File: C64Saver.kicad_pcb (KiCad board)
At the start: 2 copper layers, 33.3 x 43.2 mm, 16 parts, among them J1 Power I/O, Q1 PN2222A, Q2 PN2222A

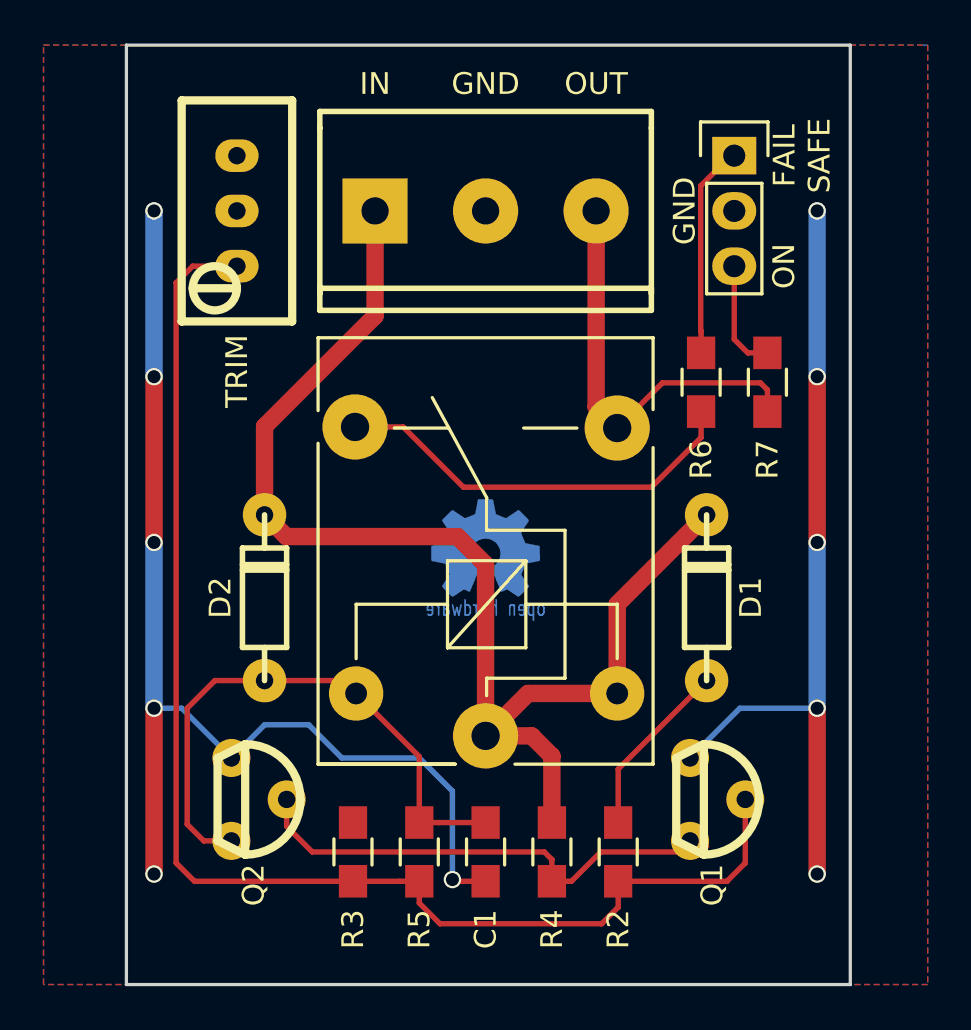
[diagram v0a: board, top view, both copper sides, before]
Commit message: Relabel some components
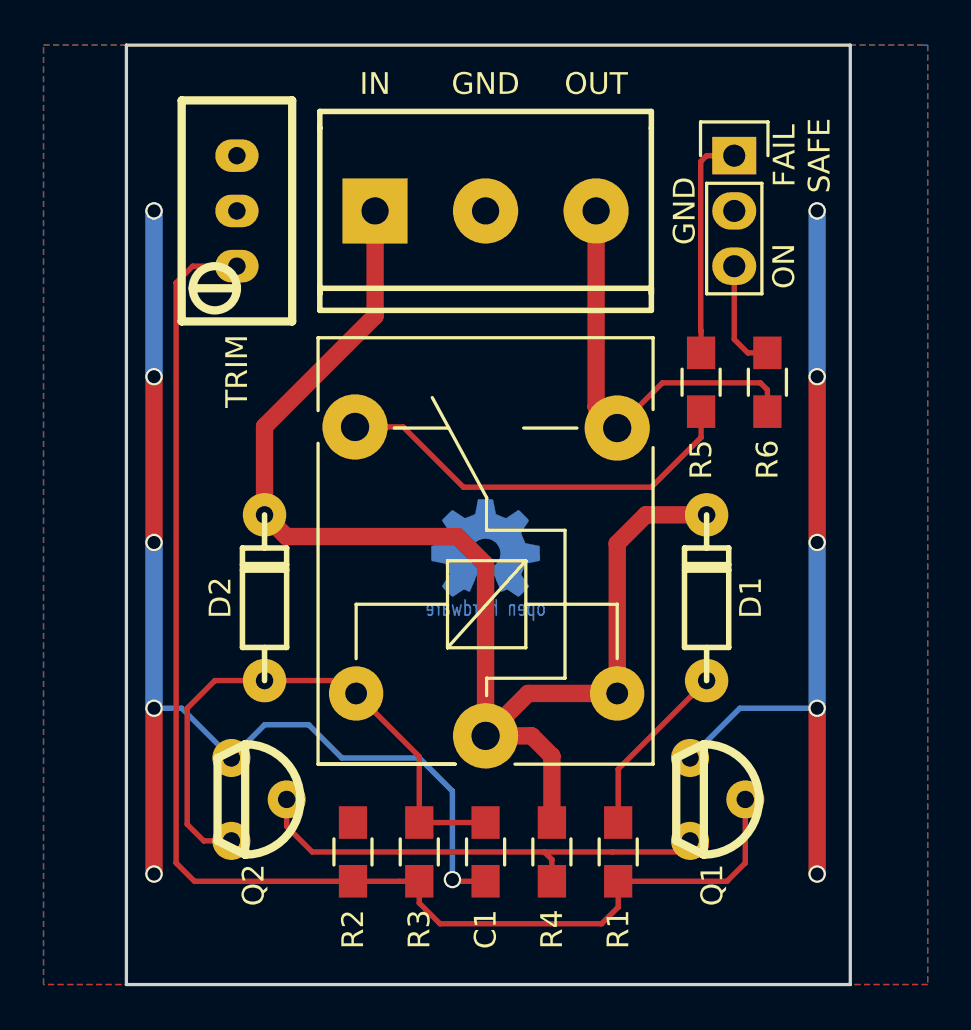
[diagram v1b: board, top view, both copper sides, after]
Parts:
- R7: renamed from R1; value R_Tuning - 5K -> 5K
- renumbered R2 to R1, R3 to R2, R5 to R3, R6 to R5, R7 to R6
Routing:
- net VCC: track 58.3 -> 60.0 mm
- net Net-(D3-Pad1): track 9.80 -> 10.5 mm
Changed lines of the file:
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@@
     (descr "trimmer, multiturn cermet, Vishay 64W")
     (tags trimmer)
-    (fp_text reference R1 (at 0 6.604 180) (layer F.SilkS) hide
+    (fp_text reference R7 (at 0 6.604 180) (layer F.SilkS) hide
       (effects (font (thickness 0.3048)))
     )
-    (fp_text value "R_Tuning - 5K" (at 4.318 0 270) (layer F.SilkS) hide
+    (fp_text value 5K (at 4.318 0 270) (layer F.SilkS) hide
       (effects (font (thickness 0.3048)))
     )
@@
     (tags "resistor 0805")
     (attr smd)
-    (fp_text reference R2 (at 3.556 0 270) (layer F.SilkS)
+    (fp_text reference R1 (at 3.556 0 270) (layer F.SilkS)
       (effects (font (size 1 1) (thickness 0.15)))
     )
@@
     (tags "resistor 0805")
     (attr smd)
-    (fp_text reference R3 (at -3.556 0 90) (layer F.SilkS)
+    (fp_text reference R2 (at -3.556 0 90) (layer F.SilkS)
       (effects (font (size 1 1) (thickness 0.15)))
     )
@@
     (tags "resistor 0805")
     (attr smd)
-    (fp_text reference R5 (at 3.556 0 270) (layer F.SilkS)
+    (fp_text reference R3 (at 3.556 0 270) (layer F.SilkS)
       (effects (font (size 1 1) (thickness 0.15)))
     )
@@
     (tags "resistor 0805")
     (attr smd)
-    (fp_text reference R6 (at -3.556 0 90) (layer F.SilkS)
+    (fp_text reference R5 (at -3.556 0 90) (layer F.SilkS)
       (effects (font (size 1 1) (thickness 0.15)))
     )
@@
     (tags "resistor 0805")
     (attr smd)
-    (fp_text reference R7 (at -3.556 0 90) (layer F.SilkS)
+    (fp_text reference R6 (at -3.556 0 90) (layer F.SilkS)
       (effects (font (size 1 1) (thickness 0.15)))
     )
@@
   (segment (start 132.08 96.52) (end 132.08 88.9) (width 0.8) (layer F.Cu) (net 2))
   (via (at 132.08 81.28) (size 0.8) (drill 0.6) (layers F.Cu B.Cu) (net 2))
+  (segment (start 153.37 103.46) (end 153.37 96.566) (width 0.8) (layer F.Cu) (net 3))
+  (segment (start 154.686 95.25) (end 157.48 95.25) (width 0.8) (layer F.Cu) (net 3))
+  (segment (start 153.37 96.566) (end 154.686 95.25) (width 0.8) (layer F.Cu) (net 3))
   (segment (start 137.16 95.25) (end 138.159489 96.249489) (width 0.8) (layer F.Cu) (net 3))
   (segment (start 137.16 91.186) (end 142.24 86.106) (width 0.8) (layer F.Cu) (net 3))
@@
   (segment (start 149.44132 105.41) (end 150.368 106.33668) (width 0.8) (layer F.Cu) (net 3))
   (segment (start 150.368 106.33668) (end 150.368 109.394) (width 0.8) (layer F.Cu) (net 3))
-  (segment (start 153.37 103.46) (end 153.37 99.36) (width 0.8) (layer F.Cu) (net 3))
   (segment (start 142.24 86.106) (end 142.24 81.28) (width 0.8) (layer F.Cu) (net 3))
-  (segment (start 153.37 99.36) (end 157.48 95.25) (width 0.8) (layer F.Cu) (net 3))
   (segment (start 153.416 106.934) (end 157.48 102.87) (width 0.25) (layer F.Cu) (net 4))
   (segment (start 153.416 109.394) (end 153.416 106.934) (width 0.25) (layer F.Cu) (net 4))
-  (segment (start 157.226 87.804) (end 157.226 86.804) (width 0.25) (layer F.Cu) (net 5))
-  (segment (start 157.226 86.804) (end 157.20899 86.78699) (width 0.25) (layer F.Cu) (net 5))
-  (segment (start 157.20899 86.78699) (end 157.20899 80.12861) (width 0.25) (layer F.Cu) (net 5))
-  (segment (start 157.20899 80.12861) (end 158.5976 78.74) (width 0.25) (layer F.Cu) (net 5))
-  (segment (start 158.5976 78.74) (end 158.75 78.74) (width 0.25) (layer F.Cu) (net 5))
+  (segment (start 158.75 78.74) (end 157.48 78.74) (width 0.25) (layer F.Cu) (net 5))
+  (segment (start 157.20899 79.01101) (end 157.20899 86.78699) (width 0.25) (layer F.Cu) (net 5))
+  (segment (start 157.48 78.74) (end 157.20899 79.01101) (width 0.25) (layer F.Cu) (net 5))
+  (segment (start 157.20899 86.78699) (end 157.226 86.804) (width 0.25) (layer F.Cu) (net 5))
+  (segment (start 157.226 86.804) (end 157.226 87.804) (width 0.25) (layer F.Cu) (net 5))
   (segment (start 153.37 91.26) (end 155.448 89.182) (width 0.25) (layer F.Cu) (net 6))
   (segment (start 155.448 89.182) (end 159.952 89.182) (width 0.25) (layer F.Cu) (net 6))
@@
   (segment (start 144.272 112.094) (end 143.372 112.094) (width 0.25) (layer F.Cu) (net 7))
   (segment (start 143.372 112.094) (end 141.224 112.094) (width 0.25) (layer F.Cu) (net 7))
-  (segment (start 150.368 112.094) (end 151.268 112.094) (width 0.25) (layer F.Cu) (net 8))
+  (segment (start 153.162 110.744) (end 156.21 110.744) (width 0.25) (layer F.Cu) (net 8))
+  (segment (start 150.018 110.744) (end 153.162 110.744) (width 0.25) (layer F.Cu) (net 8))
   (segment (start 156.21 110.744) (end 156.718 110.236) (width 0.25) (layer F.Cu) (net 8))
-  (segment (start 151.268 112.094) (end 152.618 110.744) (width 0.25) (layer F.Cu) (net 8))
-  (segment (start 152.618 110.744) (end 156.21 110.744) (width 0.25) (layer F.Cu) (net 8))
   (segment (start 138.176 108.331) (end 138.176 109.568479) (width 0.25) (layer F.Cu) (net 8))
   (segment (start 138.176 109.568479) (end 139.351521 110.744) (width 0.25) (layer F.Cu) (net 8))
@@
     (connect_pads (clearance 0.2))
     (min_thickness 0.254)
-    (fill yes (arc_segments 16) (thermal_gap 0.508) (thermal_bridge_width 0.508))
+    (fill (arc_segments 16) (thermal_gap 0.508) (thermal_bridge_width 0.508))
     (polygon
       (pts
@@
     (connect_pads (clearance 0.2))
     (min_thickness 0.254)
-    (fill yes (arc_segments 16) (thermal_gap 0.508) (thermal_bridge_width 0.508))
+    (fill (arc_segments 16) (thermal_gap 0.508) (thermal_bridge_width 0.508))
     (polygon
       (pts
